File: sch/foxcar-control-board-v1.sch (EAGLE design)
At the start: 0 parts

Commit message: Power and voltage regs done. Started current sense.
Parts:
- added C1, C21: 10u, rcl3:C-EUC0603
- added C26, C39: 22p, rcl3:C-EUC0402
- added C33, C40: 100u, rcl3:C-EUC0805
- added C38, C41: 0.1u, rcl3:C-EUC0402
- added JP1: BATT, SparkFun-Connectors:M023.5MM_LOCK
- added JP2: SERVO, SparkFun-Connectors:M03LOCK_LONGPADS
- added LED1, LED2: (no value), led:LEDCHIP-LED0603
- added R1: 11.5k, rcl3:R-EU_R0402
- added R2, R4: (no value), microbuilder:RESISTOR0402
- added R3: 19.1k, rcl3:R-EU_R0402
- added R6, R9: 500, SparkFun-Passives:RESISTOR0402-RES
- added R8: 100k, rcl3:R-EU_R0402
- added TP16, TP17, TP18, TP34, TP35, TP36, TP37, TP38: TPTP06R, testpad:TPTP06R
- added U$1: LT4619_REDUCED, LT4619:LT4619_REDUCED
- added U$3: INA169, wicker:INA169
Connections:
- new net 3.3V: C39.2, C40.1, LED2.A, TP38.TP, U$1.VOUT2
- new net 5V: C26.2, C33.1, LED1.A, TP37.TP, U$1.VOUT1
- new net GND: C1.2, C21.2, C33.2, C38.2, C40.2, C41.2, JP1.1, R1.2, R3.2, R6.1, R9.1, TP36.TP, U$1.MODE/PLLIN, U$1.PGND, U$1.SGND
- new net N$1: R2.1, U$3.VIN+
- new net N$10: TP16.TP, U$1.SW2
- new net N$14: C41.1, U$1.TK/SS2
- new net N$16: C38.1, U$1.TK/SS1
- new net N$17: LED2.C, R9.2
- new net N$19: LED1.C, R6.2
- new net N$2: C39.1, R3.1, TP35.TP, U$1.VFB2
- new net N$3: R2.2, U$3.VIN-
- new net N$4: R8.1, U$1.PGOOD
- new net N$5: C26.1, R1.1, TP34.TP, U$1.VFB1
- new net N$6: R8.2, U$1.FREQ/PLL/FLTR, U$1.INTVCC
- new net N$7: TP17.TP, U$1.SW1
- new net N$8: R4.2, U$3.GND
- new net N$9: R4.1, U$3.OUT
- new net VIN: C1.1, C21.1, JP1.2, TP18.TP, U$1.EXTVCC, U$1.VIN
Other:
- note added: "POWER"
- note added: "figure out this current/voltage sense circuit."
- note added: "insert fuse here also on/off switch"

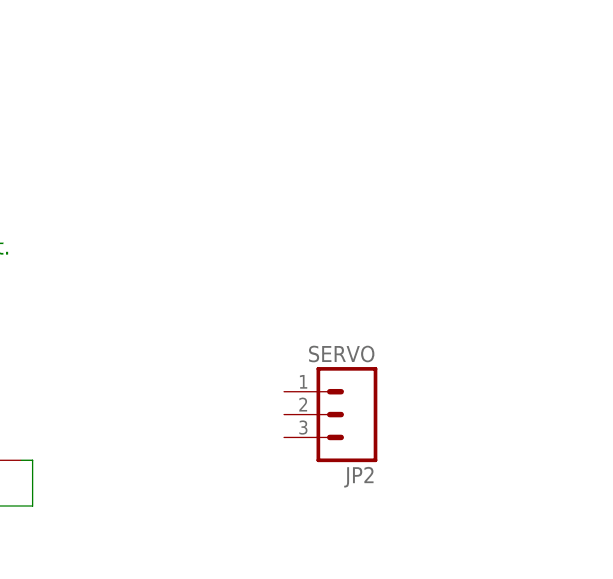
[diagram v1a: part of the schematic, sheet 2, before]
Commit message: Added IMU sensors (gyro, accel, compass) using Sparkfun references.
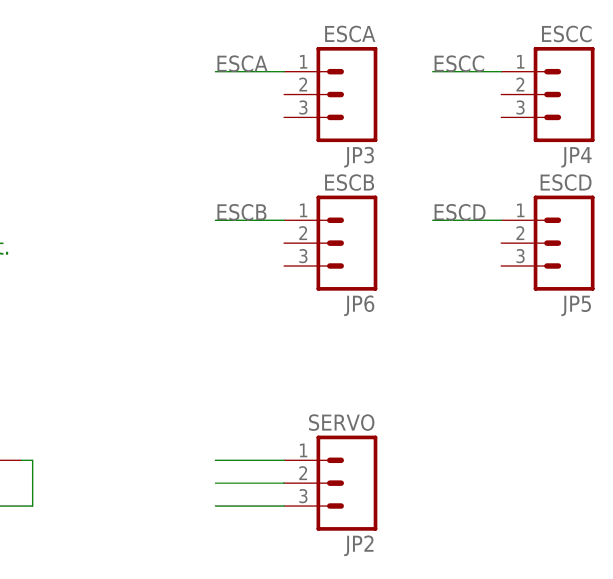
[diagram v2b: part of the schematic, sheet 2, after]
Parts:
- added C2, C7: 0.1uF, microbuilder:CAP_CERAMIC0402
- added C3, C5: 0.22uF, microbuilder:CAP_CERAMIC0402
- added C4: 4.7uF, microbuilder:CAP_CERAMIC0805
- added C6: 10nF, microbuilder:CAP_CERAMIC0402
- added C8: 2.2nF, microbuilder:CAP_CERAMIC0402
- added JP3: ESCA, SparkFun-Connectors:M03LOCK_LONGPADS
- added JP4: ESCC, SparkFun-Connectors:M03LOCK_LONGPADS
- added JP5: ESCD, SparkFun-Connectors:M03LOCK_LONGPADS
- added JP6: ESCB, SparkFun-Connectors:M03LOCK_LONGPADS
- added U$4: HMC5883LSMD, SparkFun-Sensors:HMC5883LSMD
- added U1: ADXL345, SparkFun-Sensors:ADXL345
- added U2: ITG-3200, SparkFun-Sensors:ITG-3200
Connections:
- new net ESCA: JP3.1
- new net ESCB: JP6.1
- new net ESCC: JP4.1
- new net ESCD: JP5.1
- new net N$11: JP2.1
- new net N$12: JP2.2
- new net N$13: JP2.3
- new net N$15: C6.P$1, U2.REGOUT
- new net N$20: C7.P$1, U2.CPOUT
- new net N$21: C8.P$1, U2.RESV-G
- new net N$22: C3.P$2, U$4.SETC
- new net N$23: C3.P$1, U$4.SETP
- new net N$24: C4.P$1, U$4.C1
- new net SCL: U$4.SCL, U1.SCL, U2.SCL
- new net SDA: U$4.SDA, U1.SDA, U2.SDA
- net 3.3V: now also C2.P$1, C5.P$1, U$4.S1, U$4.VDD, U$4.VDDIO, U1.CS, U1.VDD, U1.VSS, U2.VDD, U2.VLOGIC
- net GND: now also C2.P$2, C4.P$2, C5.P$2, C6.P$2, C7.P$2, C8.P$2, U$4.GND@1, U$4.GND@2, U1.GND@2, U1.GND@4, U1.GND@5, U1.SDO, U2.AD0, U2.CLKIN, U2.GND
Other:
- moved on the sheet: JP2

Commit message: Added custom STM32F4 64-pin symbol and device to layout.
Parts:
- added U$5: STM32F4R_64PIN_FOXCAR, stm32f4:STM32F4R_64PIN_FOXCAR
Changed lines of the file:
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@@
 <part name="C8" library="microbuilder" deviceset="CAP_CERAMIC" device="0402" value="2.2nF"/>
 <part name="P+6" library="SparkFun-Aesthetics" deviceset="3.3V" device=""/>
+<part name="U$5" library="stm32f4" deviceset="STM32F4R_64PIN_FOXCAR" device=""/>
 </parts>
 <sheets>
@@
 </plain>
 <instances>
+<instance part="U$5" gate="G$1" x="46.99" y="46.99"/>
 </instances>
 <busses>

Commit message: Added most of sheet 3 stm32f4 with all its connections.
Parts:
- added 25MHZ: (no value), crystal:CRYSTALCTS406
- added C20, C51, C52: 2.2uF, rcl:C-EUC0603
- added C29, C30: 16pF, rcl:C-EUC0402
- added C45, C46, C47, C48: 100nF, rcl:C-EUC0402
- added D1: (no value), SparkFun-DiscreteSemi:DIODESMA-ALT
- added JP7: (no value), SparkFun-Connectors:M06LOCK_LONGPADS
- added JTAG1: (no value), microbuilder:JTAG-CORTEXM3
- added LED37: RGB, LED_RGB_PLCC6:LED_RGB_PLCC-6
- added R17: 100, microbuilder:RESISTOR0402
- added R38, R39, R40: 10k, microbuilder:RESISTOR0402
- added R7: 1.5k, SparkFun-Passives:RESISTOR0402-RES
- added TP1, TP10, TP2, TP3, TP4, TP5, TP6, TP7, TP8, TP9: TPTP06R, testpad:TPTP06R
- added U$6: MICROSD, adafruit:MICROSD
- added USB_MICRO: USB_MICROB, SparkFun:USB_MICROB_PLUG-PTH
- added XB1: XBEE-PRO, maxstream:XBEE-PRO
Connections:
- removed net SCL: U$4.SCL, U1.SCL, U2.SCL
- removed net SDA: U$4.SDA, U1.SDA, U2.SDA
- new net BAR_GND: XB1.GND
- new net FS_DM: TP2.TP, U$5.PA11, USB_MICRO.D-
- new net FS_DP: R7.1, TP3.TP, U$5.PA12, USB_MICRO.D+
- new net FS_ID: TP4.TP, U$5.PA10, USB_MICRO.ID
- new net FS_VBUS: D1.A, TP1.TP, U$5.PA9, USB_MICRO.VCC
- new net INA: U$5.PC13
- new net INB: U$5.PC14
- new net ISENSE: U$5.PA2
- new net N$18: LED37G.A, R38.2
- new net N$25: LED37R.A, R39.2
- new net N$26: JTAG1.1, R17.1
- new net N$28: LED37B.K, U$5.PB8
- new net N$30: LED37G.K, U$5.PB9
- new net N$31: LED37R.K, U$5.PA3
- new net N$36: U$5.PC0
- new net N$37: U$5.PC1
- new net N$38: U$5.PC2
- new net N$39: U$5.PC3
- new net N$40: U$5.PC5
- new net N$41: U$5.PB0
- new net N$42: U$5.PB1
- new net N$43: U$5.PB2
- new net NRST: JTAG1.10
- new net OSC_IN: 25MHZ.2, C30.2, TP5.TP, U$5.PH0
- new net OSC_OUT: 25MHZ.1, C29.2, TP6.TP, U$5.PH1
- new net PB12: JP7.1, U$5.PB12
- new net PB13: JP7.2, U$5.PB13
- new net PB14: JP7.3, U$5.PB14
- new net PB15: JP7.4, U$5.PB15
- new net PB4: JP7.5, U$5.PB4
- new net PB5: JP7.6, U$5.PB5
- new net PHY_CLK_25MHZ: U$5.PA8
- new net PWM: U$5.PC15
- new net RXDOUT: U$5.PC7, XB1.DOUT
- new net SCL1: U$4.SCL, U$5.PB10, U1.SCL, U2.SCL
- new net SCL2: U$5.PB6
- new net SDA1: U$4.SDA, U$5.PB11, U1.SDA, U2.SDA
- new net SDA2: U$5.PB7
- new net SDIO_CLK: U$5.PC12, U$6.SCLK
- new net SDIO_CMD: U$5.PD2, U$6.DATA_IN
- new net SDIO_D0: U$5.PC8, U$6.DATA_OUT
- new net SDIO_D1: U$5.PC9, U$6.DAT1
- new net SDIO_D2: U$5.PC10, U$6.DAT2
- new net SDIO_D3: U$5.PC11, U$6.CS
- new net SERVODIR: JP2.1, U$5.PA4
- new net TCK: JTAG1.4, U$5.PA14
- new net TDI: JTAG1.8, U$5.PA15
- new net TDO: JTAG1.6, U$5.PB3
- new net TMS: JTAG1.2, U$5.PA13
- new net TXDIN: U$5.PC6, XB1.DIN/!CONFIG
- new net VSENSE: U$5.PA1
- net 3.3V: now also C20.2, C45.2, C46.2, C47.2, C48.2, C51.2, C52.2, R17.2, R38.1, R39.1, R40.1, R7.2, TP10.TP, TP9.TP, U$5.VCAP1, U$5.VCAP2, U$5.VDD1, U$5.VDD2, U$5.VDD3, U$5.VDD4, U$6.VDD, XB1.VCC, XB1.VREF
- net 5V: now also D1.C
- net ESCA: now also U$5.PA5
- net ESCB: now also U$5.PA6
- net ESCC: now also U$5.PA7
- net ESCD: now also U$5.PC4
- net GND: now also C20.1, C29.1, C30.1, C45.1, C46.1, C47.1, C48.1, C51.1, C52.1, JTAG1.3, JTAG1.5, JTAG1.9, TP7.TP, TP8.TP, U$5.VSS1, U$5.VSS2, U$6.CARD_DETECT, U$6.CARD_DETECT1, U$6.GND, U$6.GND1, U$6.VSS, USB_MICRO.GND
- net N$11: now also LED37B.A, R40.2; no longer JP2.1

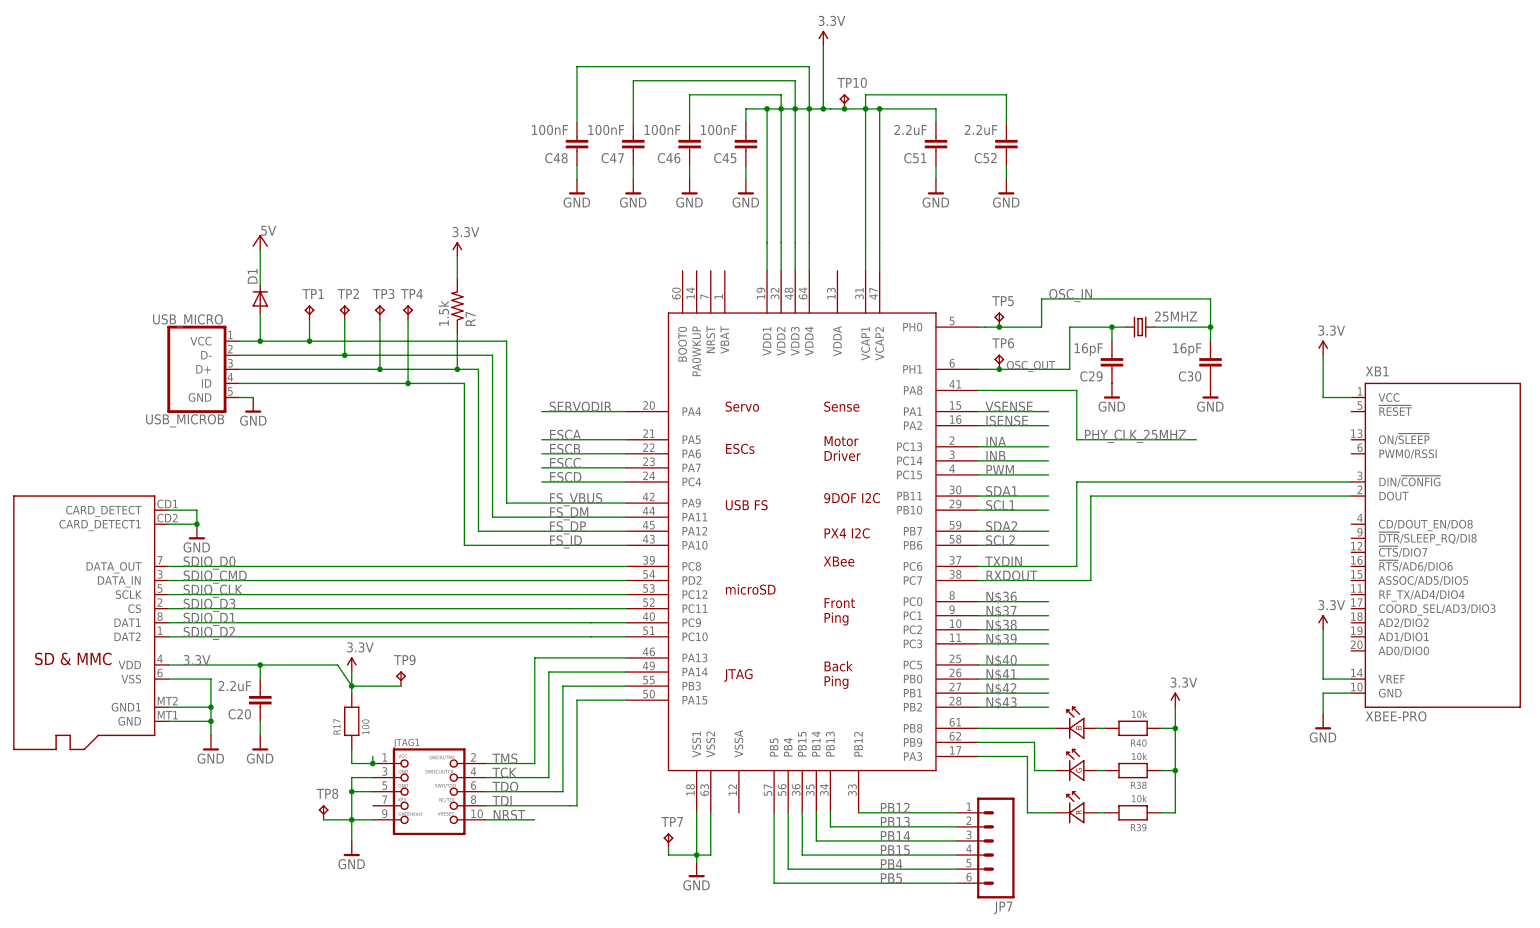
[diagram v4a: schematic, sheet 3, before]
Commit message: Tested the Maxbotix EZ4, then added it to sheet 3. Wires in place, still need Rs and Cs.
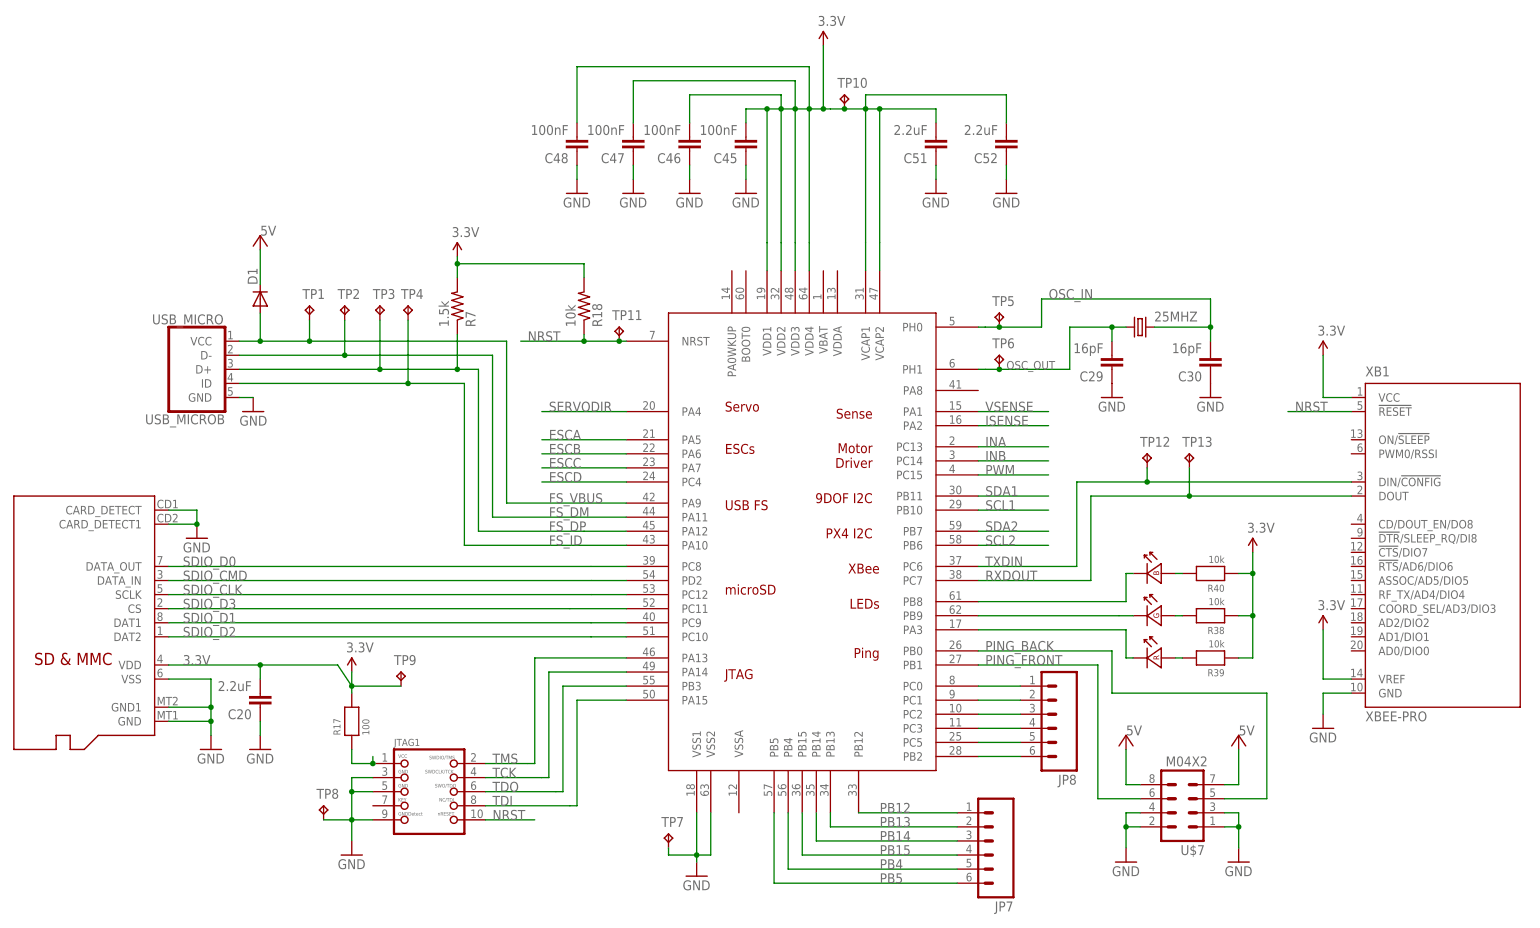
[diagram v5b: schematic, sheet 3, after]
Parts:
- added JP8: (no value), SparkFun-Connectors:M06LOCK_LONGPADS
- added R18: 10k, SparkFun-Passives:RESISTOR0402-RES
- added TP11, TP12, TP13: TPTP06R, testpad:TPTP06R
- added U$7: M04X2, SparkFun-Connectors:M04X2
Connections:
- removed net BAR_GND: XB1.GND
- removed net N$12: JP2.2
- removed net N$13: JP2.3
- removed net N$40: U$5.PC5
- removed net N$41: U$5.PB0
- removed net N$42: U$5.PB1
- removed net N$43: U$5.PB2
- removed net PHY_CLK_25MHZ: U$5.PA8
- new net N$27: JP8.5, U$5.PC5
- new net N$29: JP8.6, U$5.PB2
- new net PING_BACK: U$5.PB0, U$7.5
- new net PING_FRONT: U$5.PB1, U$7.6
- net 3.3V: now also JP2.2, R18.2
- net 5V: now also U$7.7, U$7.8
- net GND: now also JP2.3, U$7.1, U$7.2, U$7.3, U$7.4, XB1.GND
- net N$36: now also JP8.1
- net N$37: now also JP8.2
- net N$38: now also JP8.3
- net N$39: now also JP8.4
- net NRST: now also R18.1, TP11.TP, U$5.NRST, XB1.!RESET
- net RXDOUT: now also TP13.TP
- net TXDIN: now also TP12.TP
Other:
- moved on the sheet: R38, R39, R40

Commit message: Schematic done! Passes ERC.
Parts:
- removed 25MHZ: (no value), crystal:CRYSTALCTS406
- removed C2, C7: 0.1uF, microbuilder:CAP_CERAMIC0402
- removed C3, C5: 0.22uF, microbuilder:CAP_CERAMIC0402
- removed C33, C40: 100u, rcl3:C-EUC0805
- removed C38, C41: 0.1u, rcl3:C-EUC0402
- removed C39: 22p, rcl3:C-EUC0402
- removed C4: 4.7uF, microbuilder:CAP_CERAMIC0805
- removed C45, C46, C47, C48: 100nF, rcl:C-EUC0402
- removed C51, C52: 2.2uF, rcl:C-EUC0603
- removed C6: 10nF, microbuilder:CAP_CERAMIC0402
- removed D1: (no value), SparkFun-DiscreteSemi:DIODESMA-ALT
- removed JTAG1: (no value), microbuilder:JTAG-CORTEXM3
- removed LED2: (no value), led:LEDCHIP-LED0603
- removed LED37: RGB, LED_RGB_PLCC6:LED_RGB_PLCC-6
- removed R17: 100, microbuilder:RESISTOR0402
- removed R18: 10k, SparkFun-Passives:RESISTOR0402-RES
- removed R38, R39, R40: 10k, microbuilder:RESISTOR0402
- removed R7: 1.5k, SparkFun-Passives:RESISTOR0402-RES
- removed TP1, TP10, TP11, TP12, TP13, TP2, TP3, TP35, TP36, TP37, TP38, TP4, TP5, TP6, TP7, TP8, TP9: TPTP06R, testpad:TPTP06R
- removed U$1: LT4619_REDUCED, LT4619:LT4619_REDUCED
- removed U$4: HMC5883LSMD, SparkFun-Sensors:HMC5883LSMD
- removed U$5: STM32F4R_64PIN_FOXCAR, stm32f4:STM32F4R_64PIN_FOXCAR
- removed U$6: MICROSD, adafruit:MICROSD
- removed U$7: M04X2, SparkFun-Connectors:M04X2
- removed USB_MICRO: USB_MICROB, SparkFun:USB_MICROB_PLUG-PTH
- removed XB1: XBEE-PRO, maxstream:XBEE-PRO
- added C10: 47uF, SparkFun-Passives:CAP0805
- added C11, C13: 0.1uF, SparkFun-Passives:CAP0402-CAP
- added C12: 33nF, SparkFun-Passives:CAP0402-CAP
- added C14, C17, C18, C22, C25: 100nF, rcl:C-EUC0402
- added C15: 0.33uF, rcl3:C-EUC0603
- added C16: 10u, rcl3:C-EUC0603
- added C19, C9: 2.2uF, rcl:C-EUC0603
- added C23, C24: 16pF, rcl:C-EUC0402
- added C27: 4.7uF, microbuilder:CAP_CERAMIC0805
- added C28: 0.22uF, microbuilder:CAP_CERAMIC0402
- added CTS406: 25MHz, crystal:CRYSTALCTS406
- added D2: (no value), SparkFun-DiscreteSemi:DIODESMA-ALT
- added JP11: UART2, SparkFun-Connectors:M04LOCK_LONGPADS
- added JP12: I2C1-B, SparkFun-Connectors:M04LOCK_LONGPADS
- added JP13: USART3, SparkFun-Connectors:M04LOCK_LONGPADS
- added JP14: SPI1, SparkFun-Connectors:M06LOCK_LONGPADS
- added JP15: I2C1-A, SparkFun-Connectors:M04LOCK_LONGPADS
- added JP20: MOTORS, SparkFun-Connectors:M04SCREW_LOCK
- added JP21: BATT, SparkFun-Connectors:M023.5MM_LOCK
- added JP9: M10LOCK_LONGPADS, SparkFun-Connectors:M10LOCK_LONGPADS
- added JTAG2: MINI-JTAG, microbuilder:JTAG-CORTEXM3
- added LED3, LED4: (no value), led:LEDCHIP-LED0603
- added Q1: PSMN1R2-30YLC, adafruit:MOSFET-NREFLOW
- added R15: 100, microbuilder:RESISTOR0402
- added R16: 1.5k, SparkFun-Passives:RESISTOR0402-RES
- added R19, R25, R27: 10k, SparkFun-Passives:RESISTOR0402-RES
- added R20, R21, R22, R23, R24, R26: 1k, SparkFun-Passives:RESISTOR0402-RES
- added R28, R29: 4.7k, SparkFun-Passives:RESISTOR0402-RES
- added TP14, TP15, TP19, TP20, TP21, TP32, TP33, TP39, TP40, TP41, TP42, TP43: TPTP06R, testpad:TPTP06R
- added U$10: STM32F4V_100PIN_FOXCAR, stm32f4:STM32F4V_100PIN_FOXCAR
- added U$13: MICROSD, adafruit:MICROSD
- added U$8: VNH5019, wicker:VNH5019
- added USB_MICRO1: USB_MICROB, SparkFun:USB_MICROB_PLUG-PTH
- added XB2: XBEE-PRO, maxstream:XBEE-PRO
- C1: value 10u -> 100nF; device rcl3:C-EUC0603 -> rcl:C-EUC0402
- C20: value 2.2uF -> 0.22uF; device rcl:C-EUC0603 -> microbuilder:CAP_CERAMIC0402
- C21: value 10u -> 2.2uF; device rcl3:C-EUC0603 -> rcl:C-EUC0603
- C26: value 22p -> 100nF; device rcl3:C-EUC0402 -> rcl:C-EUC0402
- C29: value 16pF -> 10nF; device rcl:C-EUC0402 -> microbuilder:CAP_CERAMIC0402
- C30: value 16pF -> 0.1uF; device rcl:C-EUC0402 -> microbuilder:CAP_CERAMIC0402
- C8: value 2.2nF -> 0.1uF
- JP1: value BATT -> M10LOCK_LONGPADS; device SparkFun-Connectors:M023.5MM_LOCK -> SparkFun-Connectors:M10LOCK_LONGPADS
- JP7: value (none) -> M10LOCK_LONGPADS; device SparkFun-Connectors:M06LOCK_LONGPADS -> SparkFun-Connectors:M10LOCK_LONGPADS
- JP8: value (none) -> USART1; device SparkFun-Connectors:M06LOCK_LONGPADS -> SparkFun-Connectors:M04LOCK_LONGPADS
- LED1: value (none) -> RGB; device led:LEDCHIP-LED0603 -> LED_RGB_PLCC6:LED_RGB_PLCC-6
- R1: value 11.5k -> 270; device rcl3:R-EU_R0402 -> SparkFun-Passives:RESISTOR0402-RES
- R2, R4: value (none) -> 1.5k; device microbuilder:RESISTOR0402 -> SparkFun-Passives:RESISTOR0402-RES
- R3: value 19.1k -> 50; device rcl3:R-EU_R0402 -> SparkFun-Passives:RESISTOR0402-RES
- R6, R9: value 500 -> 10k
- R8: value 100k -> 10k; device rcl3:R-EU_R0402 -> SparkFun-Passives:RESISTOR0402-RES
- U$3: value INA169 -> MPU6000; device wicker:INA169 -> invensense:MPU-6000
- U1: value ADXL345 -> HMC5883LSMD; device SparkFun-Sensors:ADXL345 -> SparkFun-Sensors:HMC5883LSMD
- U2: value ITG-3200 -> SPX29300; device SparkFun-Sensors:ITG-3200 -> microbuilder:VREG_TO263-5
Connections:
- removed net 5V: C26.2, C33.1, D1.C, LED1.A, TP37.TP, U$1.VOUT1, U$7.7, U$7.8
- removed net INA: U$5.PC13
- removed net INB: U$5.PC14
- removed net ISENSE: U$5.PA2
- removed net N$19: LED1.C, R6.2
- removed net N$21: C8.P$1, U2.RESV-G
- removed net N$22: C3.P$2, U$4.SETC
- removed net N$23: C3.P$1, U$4.SETP
- removed net N$24: C4.P$1, U$4.C1
- removed net N$25: LED37R.A, R39.2
- removed net N$26: JTAG1.1, R17.1
- removed net N$27: JP8.5, U$5.PC5
- removed net N$28: LED37B.K, U$5.PB8
- removed net N$29: JP8.6, U$5.PB2
- removed net N$30: LED37G.K, U$5.PB9
- removed net N$31: LED37R.K, U$5.PA3
- removed net N$36: JP8.1, U$5.PC0
- removed net N$37: JP8.2, U$5.PC1
- removed net N$38: JP8.3, U$5.PC2
- removed net N$39: JP8.4, U$5.PC3
- removed net OSC_IN: 25MHZ.2, C30.2, TP5.TP, U$5.PH0
- removed net OSC_OUT: 25MHZ.1, C29.2, TP6.TP, U$5.PH1
- removed net PB12: JP7.1, U$5.PB12
- removed net PB13: JP7.2, U$5.PB13
- removed net PB14: JP7.3, U$5.PB14
- removed net PB15: JP7.4, U$5.PB15
- removed net PB4: JP7.5, U$5.PB4
- removed net PB5: JP7.6, U$5.PB5
- removed net PING_BACK: U$5.PB0, U$7.5
- removed net PING_FRONT: U$5.PB1, U$7.6
- removed net PWM: U$5.PC15
- removed net RXDOUT: TP13.TP, U$5.PC7, XB1.DOUT
- removed net SCL2: U$5.PB6
- removed net SDA2: U$5.PB7
- removed net SERVODIR: JP2.1, U$5.PA4
- removed net TXDIN: TP12.TP, U$5.PC6, XB1.DIN/!CONFIG
- removed net VSENSE: U$5.PA1
- new net DIR: JP2.1, TP21.TP, U$10.PE11
- new net IMU_CLKOUT: U$10.PD10, U$3.CLKOUT
- new net IMU_FSYNC: U$10.PD9, U$3.FSYNC
- new net IMU_INT: U$10.PD8, U$3.INT
- new net LED_B: LED1R.K, U$10.PC15
- new net LED_G: LED1G.K, U$10.PC14
- new net LED_R: LED1B.K, U$10.PC13
- new net MD_CS: C12.1, R25.1, U$10.PB1
- new net MD_CSDIS: U$10.PB0, U$8.CS_DIS
- new net MD_ENA: R20.1, U$10.PE10
- new net MD_ENB: R21.1, U$10.PE9
- new net MD_INA: R22.1, U$10.PE8
- new net MD_INB: R23.1, U$10.PE7
- new net MD_PWM: R24.1, R27.2, U$10.PB2
- new net N$12: C27.P$1, U1.C1
- new net N$13: C30.P$1, U$3.REGOUT
- new net N$41: JP9.10, U$10.PE2
- new net N$42: JP9.9, U$10.PE3
- new net N$43: JP9.8, U$10.PE4
- new net N$44: JP9.7, U$10.PE5
- new net N$45: JP9.6, U$10.PE6
- new net N$55: JP7.3, U$10.PC7
- new net N$56: JP7.4, U$10.PC6
- new net N$57: JP7.5, U$10.PD15
- new net N$58: JP7.6, U$10.PD14
- new net N$59: JP7.7, U$10.PD13
- new net N$60: JP7.8, U$10.PD12
- new net N$61: JP7.9, U$10.PD11
- new net N$66: JP1.2, U$10.PE0
- new net N$67: JP1.3, U$10.PB5
- new net N$68: JP1.4, U$10.PB4
- new net N$69: JP1.5, U$10.PD7
- new net N$70: JP1.6, U$10.PD6
- new net N$71: JP1.7, U$10.PD5
- new net N$72: JP1.8, U$10.PD4
- new net N$73: JP1.9, U$10.PD3
- new net N$74: JP1.10, U$10.PD1
- new net N$75: JP7.1, U$10.PD0
- new net N$76: R23.2, U$8.INB
- new net N$77: Q1.G, U$8.CP
- new net N$78: C10.1, C11.1, Q1.D, U$8.VCC
- new net N$79: R22.2, U$8.INA
- new net N$80: JP20.3, U$8.OUTA
- new net N$81: JP20.4, U$8.OUTB
- new net N$83: R21.2, R29.1, U$8.ENB
- new net N$84: R20.2, R28.1, U$8.ENA
- new net N$85: R24.2, U$8.PWM
- new net N$86: R25.2, R26.2, U$8.CS
- new net OSC_IN1: C24.2, CTS406.2, U$10.PH0
- new net OSC_OUT1: C23.2, CTS406.1, U$10.PH1
- new net RX1: JP8.2, U$10.PB7
- new net RX2: JP11.2, U$10.PA3
- new net RX3: JP13.2, U$10.PB11
- new net RX_DOUT1: U$10.PA1, XB2.DOUT
- new net SPI1_MISO: JP14.3, U$10.PA6
- new net SPI1_MOSI: JP14.2, U$10.PA7
- new net SPI1_NSS: JP14.5, U$10.PA4
- new net SPI1_SCK: JP14.4, U$10.PA5
- new net SPI2_CS: U$10.PB12, U$3.!CS
- new net SPI2_MISO: U$10.PB14, U$3.AD0/SDO
- new net SPI2_MOSI: U$10.PB15, U$3.SDA/SDI
- new net SPI2_SCK: U$10.PB13, U$3.SCL/SCLK
- new net TX1: JP8.3, U$10.PB6
- new net TX2: JP11.3, U$10.PA2
- new net TX3: JP13.3, U$10.PB10
- new net TX_DIN1: U$10.PA0, XB2.DIN/!CONFIG
- net 3.3V: now also C1.2, C14.2, C16.1, C17.2, C18.2, C19.2, C21.2, C22.2, C25.2, C26.2, C28.P$1, C8.P$1, C9.2, JP11.4, JP12.4, JP13.4, JP14.6, JP15.4, JP8.4, LED4.A, R15.2, R16.2, R19.2, R2.2, R28.2, R29.2, R4.2, R6.1, R8.1, R9.1, TP16.TP, TP33.TP, TP34.TP, U$10.VCAP_1, U$10.VCAP_2, U$10.VDD1, U$10.VDD2, U$10.VDD3, U$10.VDD4, U$10.VDD5, U$10.VDD6, U$10.VDDA, U$13.VDD, U$3.VDD, U1.S1, U1.VDDIO, U2.VOUT, XB2.VCC, XB2.VREF; no longer C2.P$1, C20.2, C39.2, C40.1, C45.2, C46.2, C47.2, C48.2, C5.P$1, C51.2, C52.2, LED2.A, R17.2, R18.2, R38.1, R39.1, R40.1, R7.2, TP10.TP, TP38.TP, TP9.TP, U$1.VOUT2, U$4.S1, U$4.VDD, U$4.VDDIO, U$5.VCAP1, U$5.VCAP2, U$5.VDD1, U$5.VDD2, U$5.VDD3, U$5.VDD4, U$6.VDD, U1.CS, U1.VSS, U2.VDD, U2.VLOGIC, XB1.VCC, XB1.VREF
- net ESCA: now also TP14.TP, U$10.PE15; no longer U$5.PA5
- net ESCB: now also TP15.TP, U$10.PE14; no longer U$5.PA6
- net ESCC: now also TP19.TP, U$10.PE13; no longer U$5.PA7
- net ESCD: now also TP20.TP, U$10.PE12; no longer U$5.PC4
- net FS_DM: now also TP41.TP, U$10.PA11, USB_MICRO1.D-; no longer TP2.TP, U$5.PA11, USB_MICRO.D-
- net FS_DP: now also R16.1, TP39.TP, U$10.PA12, USB_MICRO1.D+; no longer R7.1, TP3.TP, U$5.PA12, USB_MICRO.D+
- net FS_ID: now also TP42.TP, U$10.PA10, USB_MICRO1.ID; no longer TP4.TP, U$5.PA10, USB_MICRO.ID
- net FS_VBUS: now also D2.A, TP40.TP, U$10.PA9, USB_MICRO1.VCC; no longer D1.A, TP1.TP, U$5.PA9, USB_MICRO.VCC
- net GND: now also C1.1, C10.2, C11.2, C12.2, C13.2, C14.1, C15.2, C16.2, C17.1, C18.1, C19.1, C21.1, C22.1, C23.1, C24.1, C25.1, C26.1, C27.P$2, C28.P$2, C29.P$2, C30.P$2, C9.1, JP11.1, JP12.1, JP13.1, JP14.1, JP15.1, JP20.2, JP21.1, JP8.1, JTAG2.3, JTAG2.5, JTAG2.9, R1.1, R26.1, R27.1, R3.1, TP17.TP, TP32.TP, U$10.VREF+, U$10.VSS1, U$10.VSS2, U$10.VSS3, U$10.VSSA, U$13.CARD_DETECT, U$13.CARD_DETECT1, U$13.GND, U$13.GND1, U$13.VSS, U$3.CLKIN, U$3.GND, U$8.GND, U1.GND@1, U2.GND0, U2.GND1, USB_MICRO1.GND, XB2.GND; no longer C1.2, C2.P$2, C20.1, C21.2, C29.1, C30.1, C33.2, C38.2, C4.P$2, C40.2, C41.2, C45.1, C46.1, C47.1, C48.1, C5.P$2, C51.1, C52.1, C6.P$2, C7.P$2, JP1.1, JTAG1.3, JTAG1.5, JTAG1.9, R1.2, R3.2, R6.1, R9.1, TP36.TP, TP7.TP, TP8.TP, U$1.MODE/PLLIN, U$1.PGND, U$1.SGND, U$4.GND@1, U$4.GND@2, U$5.VSS1, U$5.VSS2, U$6.CARD_DETECT, U$6.CARD_DETECT1, U$6.GND, U$6.GND1, U$6.VSS, U$7.1, U$7.2, U$7.3, U$7.4, U1.GND@4, U1.GND@5, U1.SDO, U2.AD0, U2.CLKIN, U2.GND, USB_MICRO.GND, XB1.GND
- net N$1: now also JP7.2, U$10.PA8; no longer R2.1, U$3.VIN+
- net N$10: now also JP9.4, U$10.PC1; no longer TP16.TP, U$1.SW2
- net N$11: now also C20.P$1, U1.SETP; no longer LED37B.A, R40.2
- net N$14: now also JP9.3, U$10.PC2; no longer C41.1, U$1.TK/SS2
- net N$15: now also JP1.1, U$10.PE1; no longer C6.P$1, U2.REGOUT
- net N$16: now also JP9.2, U$10.PC3; no longer C38.1, U$1.TK/SS1
- net N$17: now also JP9.1, U$10.PC4; no longer LED2.C, R9.2
- net N$18: now also C29.P$1, U$3.CPOUT; no longer LED37G.A, R38.2
- net N$2: now also LED4.C, R3.2; no longer C39.1, R3.1, TP35.TP, U$1.VFB2
- net N$20: now also JTAG2.1, R15.1; no longer C7.P$1, U2.CPOUT
- net N$3: now also LED3.C, R1.2; no longer R2.2, U$3.VIN-
- net N$4: now also C20.P$2, U1.SETC; no longer R8.1, U$1.PGOOD
- net N$5: now also LED1B.A, R9.2; no longer C26.1, R1.1, TP34.TP, U$1.VFB1
- net N$6: now also LED1G.A, R6.2; no longer R8.2, U$1.FREQ/PLL/FLTR, U$1.INTVCC
- net N$7: now also LED1R.A, R8.2; no longer TP17.TP, U$1.SW1
- net N$8: now also JP7.10, U$10.PC5; no longer R4.2, U$3.GND
- net N$9: now also JP9.5, U$10.PC0; no longer R4.1, U$3.OUT
- net NRST: now also JTAG2.10, R19.1, TP43.TP, U$10.NRST, XB2.!RESET; no longer JTAG1.10, R18.1, TP11.TP, U$5.NRST, XB1.!RESET
- net SCL1: now also JP12.2, JP15.2, R4.1, U$10.PB8; no longer U$4.SCL, U$5.PB10, U2.SCL
- net SDA1: now also JP12.3, JP15.3, R2.1, U$10.PB9; no longer U$4.SDA, U$5.PB11, U2.SDA
- net SDIO_CLK: now also U$10.PC12, U$13.SCLK; no longer U$5.PC12, U$6.SCLK
- net SDIO_CMD: now also U$10.PD2, U$13.DATA_IN; no longer U$5.PD2, U$6.DATA_IN
- net SDIO_D0: now also U$10.PC8, U$13.DATA_OUT; no longer U$5.PC8, U$6.DATA_OUT
- net SDIO_D1: now also U$10.PC9, U$13.DAT1; no longer U$5.PC9, U$6.DAT1
- net SDIO_D2: now also U$10.PC10, U$13.DAT2; no longer U$5.PC10, U$6.DAT2
- net SDIO_D3: now also U$10.PC11, U$13.CS; no longer U$5.PC11, U$6.CS
- net TCK: now also JTAG2.4, U$10.PA14; no longer JTAG1.4, U$5.PA14
- net TDI: now also JTAG2.8, U$10.PA15; no longer JTAG1.8, U$5.PA15
- net TDO: now also JTAG2.6, U$10.PB3; no longer JTAG1.6, U$5.PB3
- net TMS: now also JTAG2.2, U$10.PA13; no longer JTAG1.2, U$5.PA13
- net VIN: now also C13.1, C15.1, D2.C, JP20.1, JP21.2, LED3.A, Q1.S, U$8.VBAT, U2.VIN; no longer C1.1, C21.1, JP1.2, U$1.EXTVCC, U$1.VIN
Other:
- note added: "ACCEL/GYRO"
- note added: "MAGNETOMETER"
- note added: "NC"
- note added: "VNH5019 has an internal current sense (CS)"
- note removed: "POWER"
- note removed: "figure out this current/voltage sense circuit."
- note removed: "insert fuse here also on/off switch"
